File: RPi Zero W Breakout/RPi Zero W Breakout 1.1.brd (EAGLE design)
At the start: 90 x 55 mm, 35 parts, among them J1 35RAPC4BHN2, J2 FH12-10S-0.5SH

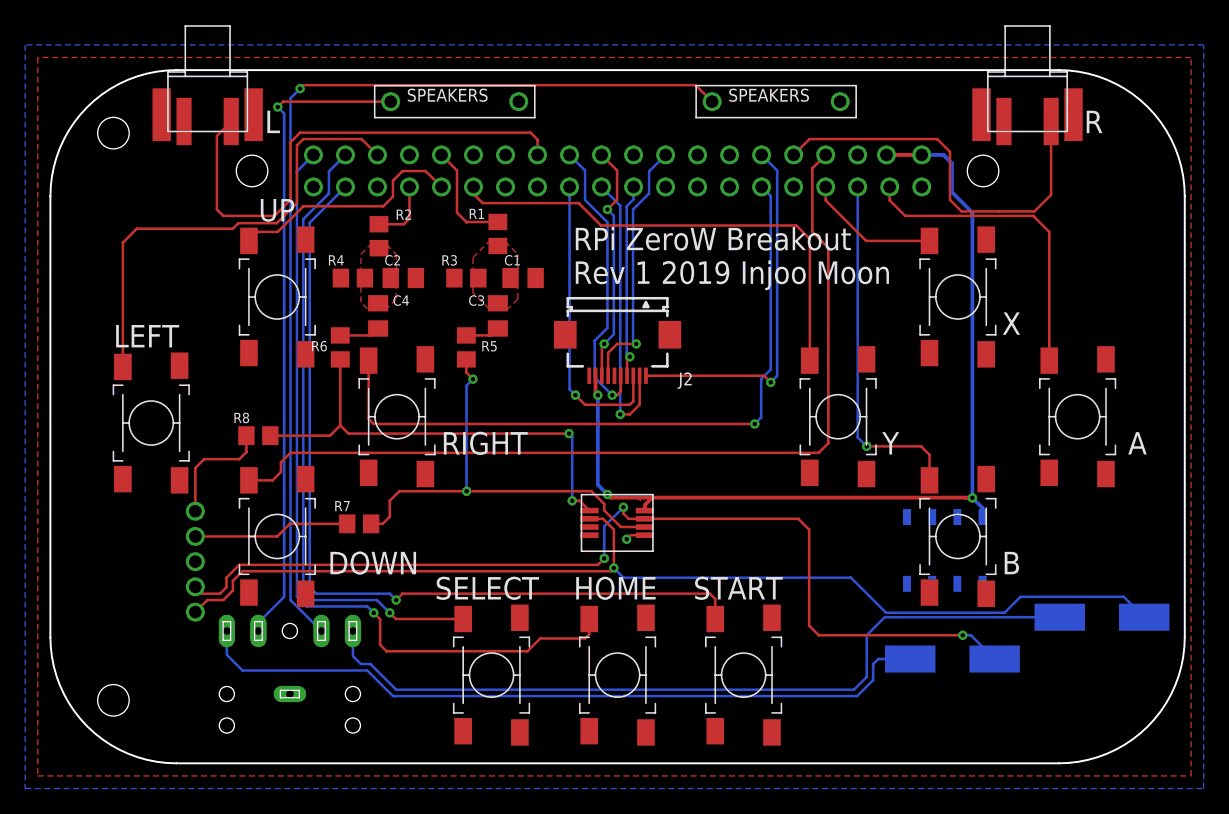
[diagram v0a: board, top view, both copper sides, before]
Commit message: Update
Moved shoulder buttons to LiPoly Management and extended LiPoly Management's dimensions. After looking at the boards in Fusion 360, I decided it would be better to have the shoulder buttons lower, rather than up high on RPi Zero Breakout. Rereouted LiPoly due to this.
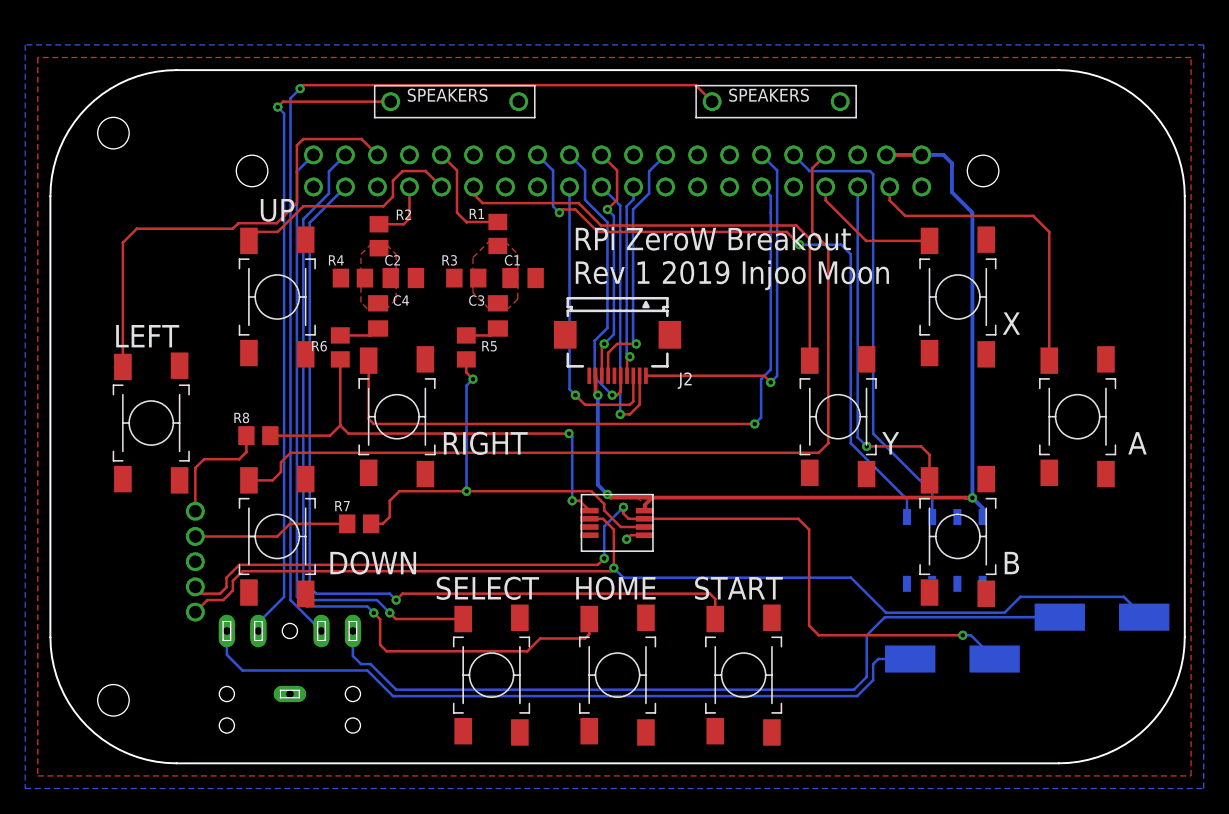
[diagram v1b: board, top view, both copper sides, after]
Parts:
- removed U$4, U$5: SPST_TACTILE_SWITCHRIGHTANGLEBENT, switches:SPST_TACTILESWITCH_TL3360CF185Q_BENTFRAME
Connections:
- net GND: no longer U$4.P$1, U$5.P$1
- net L: now also H1.P1; no longer U$4.P$2
- net R: now also H1.P2; no longer U$5.P$2
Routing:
- net L: track 40.0 -> 52.7 mm, vias 0 -> 2
- net R: track 31.9 -> 36.1 mm
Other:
- board text removed: "L"
- board text removed: "R"
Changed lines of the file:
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@@
 </layers>
 <board>
-<fusionsync huburn="a.cGVyc29uYWw6dWUyYTE1ZjVj" projecturn="a.cGVyc29uYWw6dWUyYTE1ZjVjIzIwMTgwMzEyMTIyMzg5MTU2" f3durn="urn:adsk.wipprod:dm.lineage:8GlADW5VQgCeEe4qrNd0pQ" pcbguid="c3f44bcd-ccd5-49bc-a7e4-c41e590e7a0f" lastpulledtime="" lastsyncedchangeguid="d6f20d9c-501e-470b-6ab9-3bb1b800277e"/>
+<fusionsync huburn="a.cGVyc29uYWw6dWUyYTE1ZjVj" projecturn="a.cGVyc29uYWw6dWUyYTE1ZjVjIzIwMTgwMzEyMTIyMzg5MTU2" f3durn="urn:adsk.wipprod:dm.lineage:8GlADW5VQgCeEe4qrNd0pQ" pcbguid="c3f44bcd-ccd5-49bc-a7e4-c41e590e7a0f" lastpulledtime="" lastsyncedchangeguid="5e02eddf-53c3-88de-053d-a21566df4985"/>
 <plain>
 <wire x1="10" y1="0" x2="80" y2="0" width="0.1524" layer="20"/>
@@
 Rev 1 2019 Injoo Moon</text>
 <wire x1="0" y1="45" x2="90.254" y2="45" width="0.1524" layer="47"/>
-<text x="17" y="50" size="1.778" layer="21">L</text>
-<text x="82" y="50" size="1.778" layer="21">R</text>
 </plain>
 <attributes>
@@
 <element name="SELECT" library="switches" package="SPST_TACTILESWITCH_TL3301PF160QG" value="SPST_TACTILESWITCH_TL3301PF160QG" x="35" y="7" smashed="yes" rot="R270"/>
 <element name="HOME" library="switches" package="SPST_TACTILESWITCH_TL3301PF160QG" value="SPST_TACTILESWITCH_TL3301PF160QG" x="45" y="7" smashed="yes" rot="R270"/>
-<element name="U$4" library="switches" package="SPST_TACTILESWITCH_TL3360CF185Q_BENTFRAME" value="SPST_TACTILE_SWITCHRIGHTANGLEBENT" x="12.476" y="54.5" smashed="yes">
-<attribute name="SPICEPREFIX" value="B" x="12.476" y="54.5" size="1.778" layer="27" display="off"/>
-</element>
-<element name="U$5" library="switches" package="SPST_TACTILESWITCH_TL3360CF185Q_BENTFRAME" value="SPST_TACTILE_SWITCHRIGHTANGLEBENT" x="77.524" y="54.5" smashed="yes">
-<attribute name="SPICEPREFIX" value="B" x="77.524" y="54.5" size="1.778" layer="27" display="off"/>
-</element>
 </elements>
 <signals>
@@
 <contactref element="SELECT" pad="P$1"/>
 <contactref element="START" pad="P$1"/>
-<contactref element="U$4" pad="P$1"/>
-<contactref element="U$5" pad="P$1"/>
 <wire x1="47.17" y1="18.1" x2="46.04" y2="18.1" width="0.2032" layer="1"/>
 <wire x1="46.04" y1="18.1" x2="45.72" y2="17.78" width="0.2032" layer="1"/>
@@
 <signal name="L">
 <contactref element="U$1" pad="26"/>
-<contactref element="U$4" pad="P$2"/>
-<wire x1="38.65" y1="48.27" x2="38.65" y2="49.488" width="0.2032" layer="1"/>
-<wire x1="38.65" y1="49.488" x2="38.1" y2="50.038" width="0.2032" layer="1"/>
-<wire x1="38.1" y1="50.038" x2="19.812" y2="50.038" width="0.2032" layer="1"/>
-<wire x1="19.812" y1="50.038" x2="19.05" y2="49.276" width="0.2032" layer="1"/>
-<wire x1="19.05" y1="49.276" x2="19.05" y2="44.704" width="0.2032" layer="1"/>
-<wire x1="17.78" y1="43.434" x2="19.05" y2="44.704" width="0.2032" layer="1"/>
-<wire x1="14.3485" y1="50.92" x2="13.208" y2="49.7795" width="0.2032" layer="1"/>
-<wire x1="13.208" y1="43.942" x2="13.716" y2="43.434" width="0.2032" layer="1"/>
-<wire x1="13.208" y1="49.7795" x2="13.208" y2="43.942" width="0.2032" layer="1"/>
-<wire x1="13.716" y1="43.434" x2="17.78" y2="43.434" width="0.2032" layer="1"/>
+<contactref element="H1" pad="P1"/>
+<wire x1="38.65" y1="48.27" x2="39.878" y2="47.042" width="0.2032" layer="16"/>
+<wire x1="39.878" y1="44.196" x2="40.386" y2="43.688" width="0.2032" layer="16"/>
+<via x="40.386" y="43.688" extent="1-16" drill="0.35"/>
+<wire x1="40.386" y1="43.688" x2="40.64" y2="43.942" width="0.2032" layer="1"/>
+<wire x1="58.42" y1="42.164" x2="59.436" y2="41.148" width="0.2032" layer="1"/>
+<via x="59.436" y="41.148" extent="1-16" drill="0.35"/>
+<wire x1="39.878" y1="47.042" x2="39.878" y2="44.196" width="0.2032" layer="16"/>
+<wire x1="40.64" y1="43.942" x2="41.656" y2="43.942" width="0.2032" layer="1"/>
+<wire x1="41.656" y1="43.942" x2="43.434" y2="42.164" width="0.2032" layer="1"/>
+<wire x1="43.434" y1="42.164" x2="58.42" y2="42.164" width="0.2032" layer="1"/>
+<wire x1="59.436" y1="41.148" x2="62.738" y2="41.148" width="0.2032" layer="16"/>
+<wire x1="62.738" y1="41.148" x2="63.5" y2="40.386" width="0.2032" layer="16"/>
+<wire x1="63.5" y1="25.4" x2="63.5" y2="40.386" width="0.2032" layer="16"/>
+<wire x1="67.96" y1="19.54" x2="67.96" y2="20.94" width="0.2032" layer="16"/>
+<wire x1="67.96" y1="20.94" x2="63.5" y2="25.4" width="0.2032" layer="16"/>
 </signal>
 <signal name="DOWN">
@@
 <signal name="R">
 <contactref element="U$1" pad="10"/>
-<contactref element="U$5" pad="P$2"/>
-<wire x1="58.97" y1="48.27" x2="60.23" y2="49.53" width="0.2032" layer="1"/>
-<wire x1="70.358" y1="49.53" x2="71.374" y2="48.514" width="0.2032" layer="1"/>
-<wire x1="71.374" y1="48.514" x2="71.374" y2="44.704" width="0.2032" layer="1"/>
-<wire x1="71.374" y1="44.704" x2="72.2884" y2="43.7896" width="0.2032" layer="1"/>
-<wire x1="60.23" y1="49.53" x2="70.358" y2="49.53" width="0.2032" layer="1"/>
-<wire x1="72.2884" y1="43.7896" x2="75.2856" y2="43.7896" width="0.2032" layer="1"/>
-<wire x1="79.3965" y1="45.1065" x2="78.0796" y2="43.7896" width="0.2032" layer="1"/>
-<wire x1="79.3965" y1="50.92" x2="79.3965" y2="45.1065" width="0.2032" layer="1"/>
-<wire x1="78.0796" y1="43.7896" x2="75.2856" y2="43.7896" width="0.2032" layer="1"/>
+<contactref element="H1" pad="P2"/>
+<wire x1="58.97" y1="48.27" x2="60.198" y2="47.042" width="0.2032" layer="16"/>
+<wire x1="60.198" y1="47.042" x2="60.198" y2="46.99" width="0.2032" layer="16"/>
+<wire x1="60.198" y1="46.99" x2="65.024" y2="46.99" width="0.2032" layer="16"/>
+<wire x1="65.024" y1="46.99" x2="65.278" y2="46.736" width="0.2032" layer="16"/>
+<wire x1="69.96" y1="21.48" x2="69.96" y2="19.54" width="0.2032" layer="16"/>
+<wire x1="65.278" y1="46.736" x2="65.278" y2="26.162" width="0.2032" layer="16"/>
+<wire x1="65.278" y1="26.162" x2="69.96" y2="21.48" width="0.2032" layer="16"/>
 </signal>
 <signal name="LEFT">
